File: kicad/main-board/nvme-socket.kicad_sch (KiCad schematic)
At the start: 8 parts, among them J5 Bus_M.2_Socket_M, U11 TPS22918DBVR

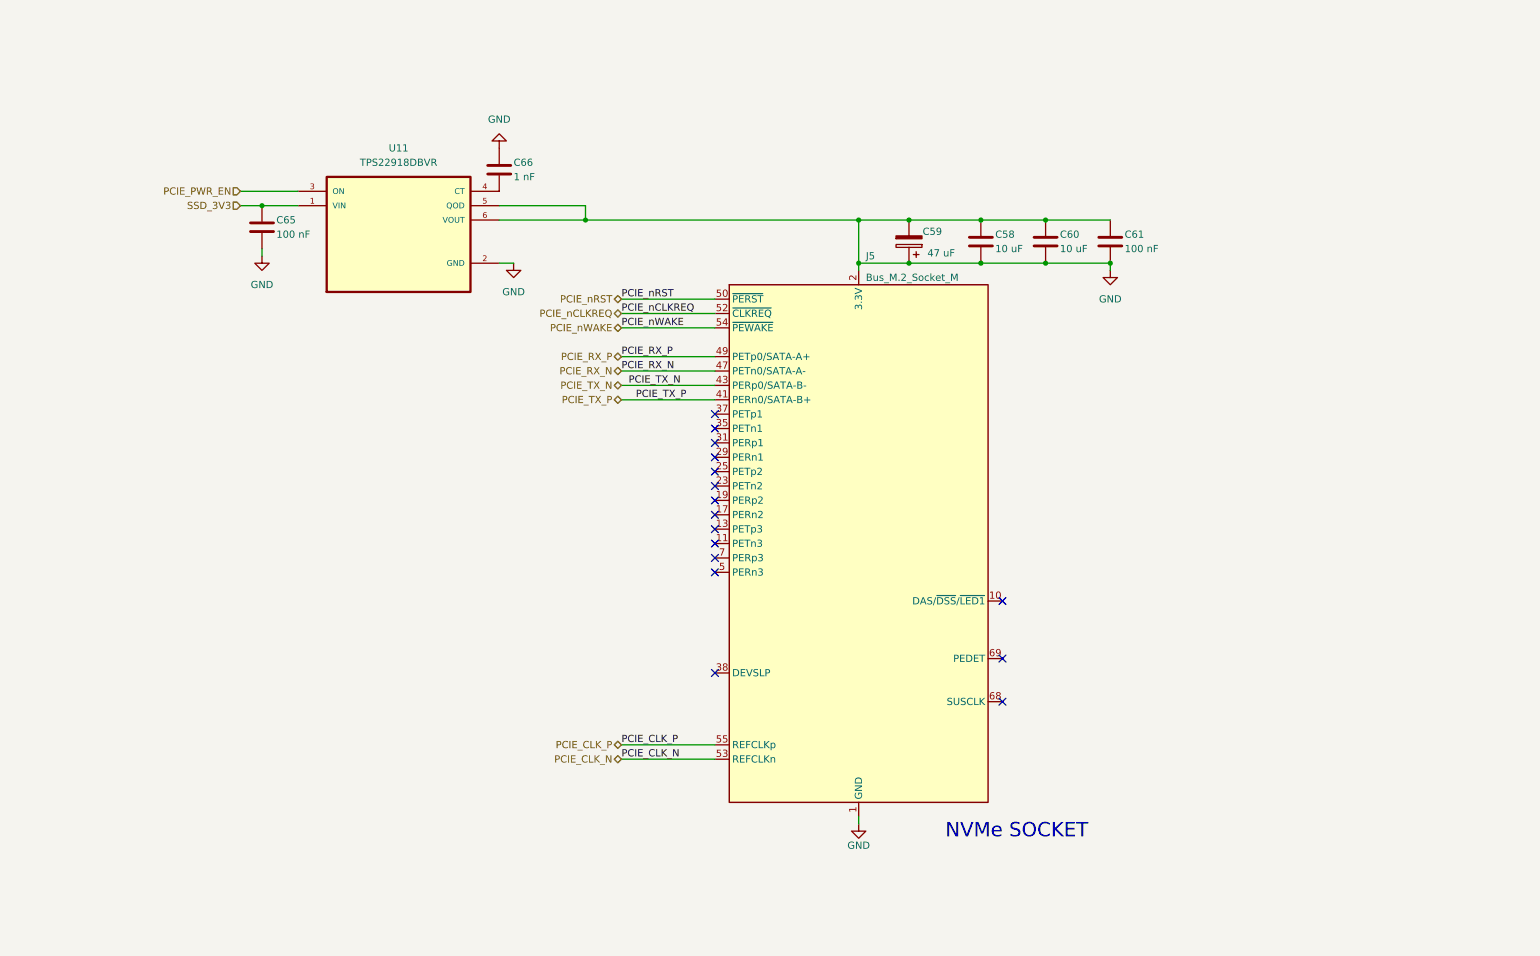
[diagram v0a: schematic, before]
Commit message: Completed the main board schematic
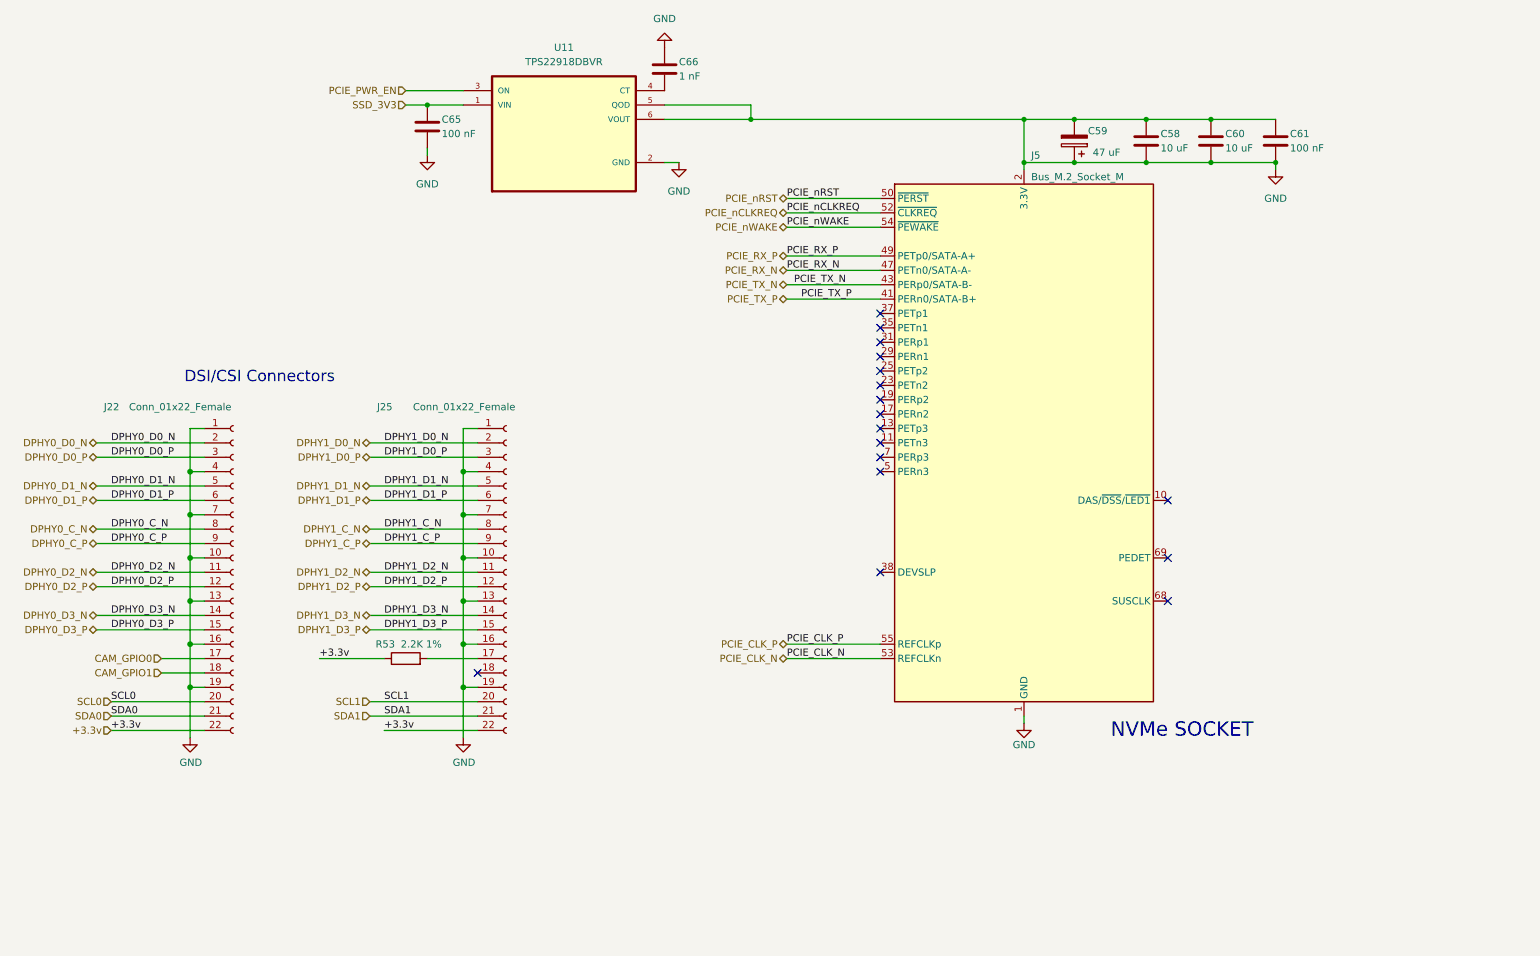
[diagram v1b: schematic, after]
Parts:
- added J22, J25: Conn_01x22_Female, CM5IO:Hirose_FH12-22S-0.5SH_1x22-1MP_P0.50mm_Horizontal, symbol Connector:Conn_01x22_Socket
- added R53: 2.2K 1%, Resistor_SMD:R_0402_1005Metric, symbol Device:R
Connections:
- net GND: now also J22.1 (Pin_1), J22.10 (Pin_10), J22.13 (Pin_13), J22.16 (Pin_16), J22.19 (Pin_19), J22.4 (Pin_4), J22.7 (Pin_7), J25.1 (Pin_1), J25.10 (Pin_10), J25.13 (Pin_13), J25.16 (Pin_16), J25.19 (Pin_19), J25.4 (Pin_4), J25.7 (Pin_7)
- new net: J25.17 (Pin_17), R53.2
- new net +3.3v: J22.22 (Pin_22), J25.22 (Pin_22), R53.1
- new net CAM_GPIO0: J22.17 (Pin_17)
- new net CAM_GPIO1: J22.18 (Pin_18)
- new net DPHY0_C_N: J22.8 (Pin_8)
- new net DPHY0_C_P: J22.9 (Pin_9)
- new net DPHY0_D0_N: J22.2 (Pin_2)
- new net DPHY0_D0_P: J22.3 (Pin_3)
- new net DPHY0_D1_N: J22.5 (Pin_5)
- new net DPHY0_D1_P: J22.6 (Pin_6)
- new net DPHY0_D2_N: J22.11 (Pin_11)
- new net DPHY0_D2_P: J22.12 (Pin_12)
- new net DPHY0_D3_N: J22.14 (Pin_14)
- new net DPHY0_D3_P: J22.15 (Pin_15)
- new net DPHY1_C_N: J25.8 (Pin_8)
- new net DPHY1_C_P: J25.9 (Pin_9)
- new net DPHY1_D0_N: J25.2 (Pin_2)
- new net DPHY1_D0_P: J25.3 (Pin_3)
- new net DPHY1_D1_N: J25.5 (Pin_5)
- new net DPHY1_D1_P: J25.6 (Pin_6)
- new net DPHY1_D2_N: J25.11 (Pin_11)
- new net DPHY1_D2_P: J25.12 (Pin_12)
- new net DPHY1_D3_N: J25.14 (Pin_14)
- new net DPHY1_D3_P: J25.15 (Pin_15)
- new net SCL0: J22.20 (Pin_20)
- new net SCL1: J25.20 (Pin_20)
- new net SDA0: J22.21 (Pin_21)
- new net SDA1: J25.21 (Pin_21)
- no-connect marks 16 -> 17
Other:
- note added: "DSI/CSI Connectors"
- moved on the sheet: C58, C59, C60, C61, C65, C66, J5, U11

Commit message: finally completed the schematic
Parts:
- renumbered C66 to C79, C65 to C80, C59 to C81, C58 to C82, C60 to C83, C61 to C84, J5 to J45, J22 to J46, J25 to J47, R53 to R69, U11 to U22
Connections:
- net GND: no longer C81.1, C82.1, C83.1, C84.1, J45.12 (3.3V), J45.14 (3.3V), J45.16 (3.3V), J45.18 (3.3V), J45.2 (3.3V), J45.4 (3.3V), J45.70 (3.3V), J45.72 (3.3V), J45.74 (3.3V), U22.5 (QOD), U22.6 (VOUT)
- net SSD_3V3 renamed SSD_3V
- new net: C81.1, C82.1, C83.1, C84.1, J45.12 (3.3V), J45.14 (3.3V), J45.16 (3.3V), J45.18 (3.3V), J45.2 (3.3V), J45.4 (3.3V), J45.70 (3.3V), J45.72 (3.3V), J45.74 (3.3V), U22.5 (QOD), U22.6 (VOUT)
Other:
- note added: "CIPHER - by ARYAN-GIT-BYTE"
- moved on the sheet: C81
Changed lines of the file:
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@@
 		(effects
 			(font
+				(face "Arial Black")
 				(size 2.0066 2.0066)
 			)
@@
 		(effects
 			(font
-				(face "KiCad Font")
+				(face "Arial Black")
 				(size 2.54 2.54)
 			)
 		)
 	)
+	(text "CIPHER - by ARYAN-GIT-BYTE\n"
+		(exclude_from_sim no)
+		(at 230.886 173.736 0)
+		(effects
+			(font
+				(face "Clarendon Lt BT")
+				(size 5.08 5.08)
+			)
+		)
+	)
 	(junction
 		(at 63.5 133.35)
@@
 	)
 	(junction
-		(at 210.82 40.64)
-		(diameter 0)
-		(color 0 0 0 0)
-	)
-	(junction
 		(at 63.5 125.73)
 		(diameter 1.016)
@@
 	)
 	(junction
-		(at 219.71 40.64)
+		(at 219.71 33.02)
 		(diameter 0)
 		(color 0 0 0 0)
@@
 	)
 	(junction
-		(at 219.71 33.02)
-		(diameter 0)
-		(color 0 0 0 0)
-	)
-	(junction
 		(at 111.76 102.87)
 		(diameter 1.016)
@@
 	(wire
 		(pts
-			(xy 219.71 33.02) (xy 232.41 33.02)
-		)
-		(stroke
-			(width 0)
-			(type default)
-		)
-	)
-	(wire
-		(pts
 			(xy 168.91 57.15) (xy 185.42 57.15)
 		)
@@
 	(wire
 		(pts
-			(xy 147.32 30.48) (xy 162.56 30.48)
-		)
-		(stroke
-			(width 0)
-			(type default)
-		)
-	)
-	(wire
-		(pts
 			(xy 95.25 113.03) (xy 114.3 113.03)
 		)
@@
 	(wire
 		(pts
-			(xy 210.82 40.64) (xy 219.71 40.64)
-		)
-		(stroke
-			(width 0)
-			(type default)
-		)
-	)
-	(wire
-		(pts
 			(xy 111.76 133.35) (xy 111.76 142.24)
 		)
@@
 	(wire
 		(pts
+			(xy 147.32 30.48) (xy 162.56 30.48)
+		)
+		(stroke
+			(width 0)
+			(type default)
+		)
+	)
+	(wire
+		(pts
 			(xy 63.5 125.73) (xy 66.04 125.73)
 		)
@@
 	(wire
 		(pts
-			(xy 210.82 33.02) (xy 210.82 40.64)
+			(xy 46.99 92.71) (xy 66.04 92.71)
 		)
 		(stroke
 			(width 0)
-			(type default)
+			(type solid)
 		)
 	)
 	(wire
 		(pts
-			(xy 46.99 92.71) (xy 66.04 92.71)
+			(xy 101.6 27.94) (xy 111.76 27.94)
 		)
 		(stroke
 			(width 0)
-			(type solid)
+			(type default)
 		)
 	)
 	(wire
 		(pts
-			(xy 101.6 27.94) (xy 111.76 27.94)
+			(xy 66.04 135.89) (xy 49.53 135.89)
 		)
 		(stroke
 			(width 0)
-			(type default)
+			(type solid)
 		)
 	)
 	(wire
 		(pts
-			(xy 66.04 135.89) (xy 49.53 135.89)
+			(xy 210.82 33.02) (xy 210.82 41.91)
 		)
 		(stroke
 			(width 0)
-			(type solid)
+			(type default)
 		)
 	)
 	(wire
 		(pts
-			(xy 210.82 40.64) (xy 210.82 41.91)
+			(xy 219.71 33.02) (xy 232.41 33.02)
 		)
 		(stroke
@@
 		)
 	)
-	(hierarchical_label "SSD_3V3"
+	(hierarchical_label "SSD_3V"
 		(shape input)
 		(at 101.6 30.48 180)
@@
 		(on_board yes)
 		(dnp no)
-		(property "Reference" "#PWR0134"
+		(property "Reference" "#PWR0129"
 			(at 63.5 148.59 0)
 			(effects
@@
 			(project "OVERALL"
 				(path "/0e81c85d-86ab-4d5d-8c59-60b8e6f89475/b23c6cec-f7d8-4bb5-9180-0d1142d1aed0/eea0b253-8fa4-41dd-9ad3-ca52a23a8c16/ed4211b6-8245-4b09-acae-1cf19e5170b7"
-					(reference "#PWR0134")
+					(reference "#PWR0129")
 					(unit 1)
 				)
@@
 		(on_board yes)
 		(dnp no)
-		(property "Reference" "#PWR0135"
+		(property "Reference" "#PWR0130"
 			(at 111.76 148.59 0)
 			(effects
@@
 			(project "OVERALL"
 				(path "/0e81c85d-86ab-4d5d-8c59-60b8e6f89475/b23c6cec-f7d8-4bb5-9180-0d1142d1aed0/eea0b253-8fa4-41dd-9ad3-ca52a23a8c16/ed4211b6-8245-4b09-acae-1cf19e5170b7"
-					(reference "#PWR0135")
+					(reference "#PWR0130")
 					(unit 1)
 				)
@@
 		(on_board yes)
 		(dnp no)
-		(property "Reference" "R53"
+		(property "Reference" "R69"
 			(at 99.695 125.73 90)
 			(effects
@@
 			(project "OVERALL"
 				(path "/0e81c85d-86ab-4d5d-8c59-60b8e6f89475/b23c6cec-f7d8-4bb5-9180-0d1142d1aed0/eea0b253-8fa4-41dd-9ad3-ca52a23a8c16/ed4211b6-8245-4b09-acae-1cf19e5170b7"
-					(reference "R53")
+					(reference "R69")
 					(unit 1)
 				)
@@
 		(on_board yes)
 		(dnp no)
-		(property "Reference" "C65"
+		(property "Reference" "C80"
 			(at 107.95 33.02 0)
 			(effects
@@
 			(project "OVERALL"
 				(path "/0e81c85d-86ab-4d5d-8c59-60b8e6f89475/b23c6cec-f7d8-4bb5-9180-0d1142d1aed0/eea0b253-8fa4-41dd-9ad3-ca52a23a8c16/ed4211b6-8245-4b09-acae-1cf19e5170b7"
-					(reference "C65")
+					(reference "C80")
 					(unit 1)
 				)
@@
 		(dnp no)
 		(fields_autoplaced yes)
-		(property "Reference" "#PWR067"
+		(property "Reference" "#PWR0116"
 			(at 149.86 46.99 0)
 			(effects
@@
 			(project ""
 				(path "/0e81c85d-86ab-4d5d-8c59-60b8e6f89475/b23c6cec-f7d8-4bb5-9180-0d1142d1aed0/eea0b253-8fa4-41dd-9ad3-ca52a23a8c16/ed4211b6-8245-4b09-acae-1cf19e5170b7"
-					(reference "#PWR067")
+					(reference "#PWR0116")
 					(unit 1)
 				)
@@
 		(dnp no)
 		(fields_autoplaced yes)
-		(property "Reference" "#PWR059"
+		(property "Reference" "#PWR0117"
 			(at 255.27 48.26 0)
 			(effects
@@
 			(project ""
 				(path "/0e81c85d-86ab-4d5d-8c59-60b8e6f89475/b23c6cec-f7d8-4bb5-9180-0d1142d1aed0/eea0b253-8fa4-41dd-9ad3-ca52a23a8c16/ed4211b6-8245-4b09-acae-1cf19e5170b7"
-					(reference "#PWR059")
+					(reference "#PWR0117")
 					(unit 1)
 				)
@@
 		(on_board yes)
 		(dnp no)
-		(property "Reference" "#PWR057"
+		(property "Reference" "#PWR0128"
 			(at 210.82 146.05 0)
 			(effects
@@
 			(project ""
 				(path "/0e81c85d-86ab-4d5d-8c59-60b8e6f89475/b23c6cec-f7d8-4bb5-9180-0d1142d1aed0/eea0b253-8fa4-41dd-9ad3-ca52a23a8c16/ed4211b6-8245-4b09-acae-1cf19e5170b7"
-					(reference "#PWR057")
+					(reference "#PWR0128")
 					(unit 1)
 				)
@@
 	(symbol
 		(lib_id "Device:C_Polarized")
-		(at 219.71 36.83 180)
+		(at 219.71 36.83 0)
 		(unit 1)
 		(exclude_from_sim no)
@@
 		(on_board yes)
 		(dnp no)
-		(property "Reference" "C59"
-			(at 225.552 35.052 0)
+		(property "Reference" "C81"
+			(at 220.726 34.798 0)
 			(effects
 				(font
@@
 		)
 		(property "Value" "47 uF"
-			(at 227.838 38.862 0)
+			(at 219.964 39.116 0)
 			(effects
 				(font
@@
 		)
 		(property "Footprint" ""
-			(at 218.7448 33.02 0)
+			(at 220.6752 40.64 0)
 			(effects
 				(font
@@
 			(project ""
 				(path "/0e81c85d-86ab-4d5d-8c59-60b8e6f89475/b23c6cec-f7d8-4bb5-9180-0d1142d1aed0/eea0b253-8fa4-41dd-9ad3-ca52a23a8c16/ed4211b6-8245-4b09-acae-1cf19e5170b7"
-					(reference "C59")
+					(reference "C81")
 					(unit 1)
 				)
@@
 		(dnp no)
 		(fields_autoplaced yes)
-		(property "Reference" "#PWR069"
+		(property "Reference" "#PWR0112"
 			(at 147.32 13.97 0)
 			(effects
@@
 			(project ""
 				(path "/0e81c85d-86ab-4d5d-8c59-60b8e6f89475/b23c6cec-f7d8-4bb5-9180-0d1142d1aed0/eea0b253-8fa4-41dd-9ad3-ca52a23a8c16/ed4211b6-8245-4b09-acae-1cf19e5170b7"
-					(reference "#PWR069")
+					(reference "#PWR0112")
 					(unit 1)
 				)
@@
 		(on_board yes)
 		(dnp no)
-		(property "Reference" "J22"
+		(property "Reference" "J46"
 			(at 48.26 83.82 0)
 			(effects
@@
 			(project "OVERALL"
 				(path "/0e81c85d-86ab-4d5d-8c59-60b8e6f89475/b23c6cec-f7d8-4bb5-9180-0d1142d1aed0/eea0b253-8fa4-41dd-9ad3-ca52a23a8c16/ed4211b6-8245-4b09-acae-1cf19e5170b7"
-					(reference "J22")
+					(reference "J46")
 					(unit 1)
 				)
@@
 		(on_board yes)
 		(dnp no)
-		(property "Reference" "J5"
+		(property "Reference" "J45"
 			(at 212.09 39.37 0)
 			(effects
@@
 			(project ""
 				(path "/0e81c85d-86ab-4d5d-8c59-60b8e6f89475/b23c6cec-f7d8-4bb5-9180-0d1142d1aed0/eea0b253-8fa4-41dd-9ad3-ca52a23a8c16/ed4211b6-8245-4b09-acae-1cf19e5170b7"
-					(reference "J5")
+					(reference "J45")
 					(unit 1)
 				)
@@
 		(on_board yes)
 		(dnp no)
-		(property "Reference" "J25"
+		(property "Reference" "J47"
 			(at 96.52 83.82 0)
 			(effects
@@
 			(project "OVERALL"
 				(path "/0e81c85d-86ab-4d5d-8c59-60b8e6f89475/b23c6cec-f7d8-4bb5-9180-0d1142d1aed0/eea0b253-8fa4-41dd-9ad3-ca52a23a8c16/ed4211b6-8245-4b09-acae-1cf19e5170b7"
-					(reference "J25")
+					(reference "J47")
 					(unit 1)
 				)
@@
 		(on_board yes)
 		(dnp no)
-		(property "Reference" "C66"
+		(property "Reference" "C79"
 			(at 149.86 22.86 0)
 			(effects
@@
 			(project "OVERALL"
 				(path "/0e81c85d-86ab-4d5d-8c59-60b8e6f89475/b23c6cec-f7d8-4bb5-9180-0d1142d1aed0/eea0b253-8fa4-41dd-9ad3-ca52a23a8c16/ed4211b6-8245-4b09-acae-1cf19e5170b7"
-					(reference "C66")
+					(reference "C79")
 					(unit 1)
 				)
@@
 		(on_board yes)
 		(dnp no)
-		(property "Reference" "C60"
+		(property "Reference" "C83"
 			(at 246.38 35.56 0)
 			(effects
@@
 			(project "OVERALL"
 				(path "/0e81c85d-86ab-4d5d-8c59-60b8e6f89475/b23c6cec-f7d8-4bb5-9180-0d1142d1aed0/eea0b253-8fa4-41dd-9ad3-ca52a23a8c16/ed4211b6-8245-4b09-acae-1cf19e5170b7"
-					(reference "C60")
+					(reference "C83")
 					(unit 1)
 				)
@@
 		(dnp no)
 		(fields_autoplaced yes)
-		(property "Reference" "#PWR068"
+		(property "Reference" "#PWR0115"
 			(at 105.41 45.72 0)
 			(effects
@@
 			(project ""
 				(path "/0e81c85d-86ab-4d5d-8c59-60b8e6f89475/b23c6cec-f7d8-4bb5-9180-0d1142d1aed0/eea0b253-8fa4-41dd-9ad3-ca52a23a8c16/ed4211b6-8245-4b09-acae-1cf19e5170b7"
-					(reference "#PWR068")
+					(reference "#PWR0115")
 					(unit 1)
 				)
@@
 		(on_board yes)
 		(dnp no)
-		(property "Reference" "C58"
+		(property "Reference" "C82"
 			(at 234.95 35.56 0)
 			(effects
@@
 			(project ""
 				(path "/0e81c85d-86ab-4d5d-8c59-60b8e6f89475/b23c6cec-f7d8-4bb5-9180-0d1142d1aed0/eea0b253-8fa4-41dd-9ad3-ca52a23a8c16/ed4211b6-8245-4b09-acae-1cf19e5170b7"
-					(reference "C58")
+					(reference "C82")
 					(unit 1)
 				)
@@
 		(dnp no)
 		(fields_autoplaced yes)
-		(property "Reference" "U11"
+		(property "Reference" "U22"
 			(at 129.54 20.32 0)
 			(effects
@@
 			(project ""
 				(path "/0e81c85d-86ab-4d5d-8c59-60b8e6f89475/b23c6cec-f7d8-4bb5-9180-0d1142d1aed0/eea0b253-8fa4-41dd-9ad3-ca52a23a8c16/ed4211b6-8245-4b09-acae-1cf19e5170b7"
-					(reference "U11")
+					(reference "U22")
 					(unit 1)
 				)
@@
 		(on_board yes)
 		(dnp no)
-		(property "Reference" "C61"
+		(property "Reference" "C84"
 			(at 257.81 35.56 0)
 			(effects
@@
 			(project "OVERALL"
 				(path "/0e81c85d-86ab-4d5d-8c59-60b8e6f89475/b23c6cec-f7d8-4bb5-9180-0d1142d1aed0/eea0b253-8fa4-41dd-9ad3-ca52a23a8c16/ed4211b6-8245-4b09-acae-1cf19e5170b7"
-					(reference "C61")
+					(reference "C84")
 					(unit 1)
 				)

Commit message: DOCUMENTED Till the Navigation board
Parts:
- renumbered C79 to C89, C80 to C90, C81 to C91, C82 to C92, C83 to C93, C84 to C94, J45 to J50, J46 to J51, J47 to J52, U22 to U24

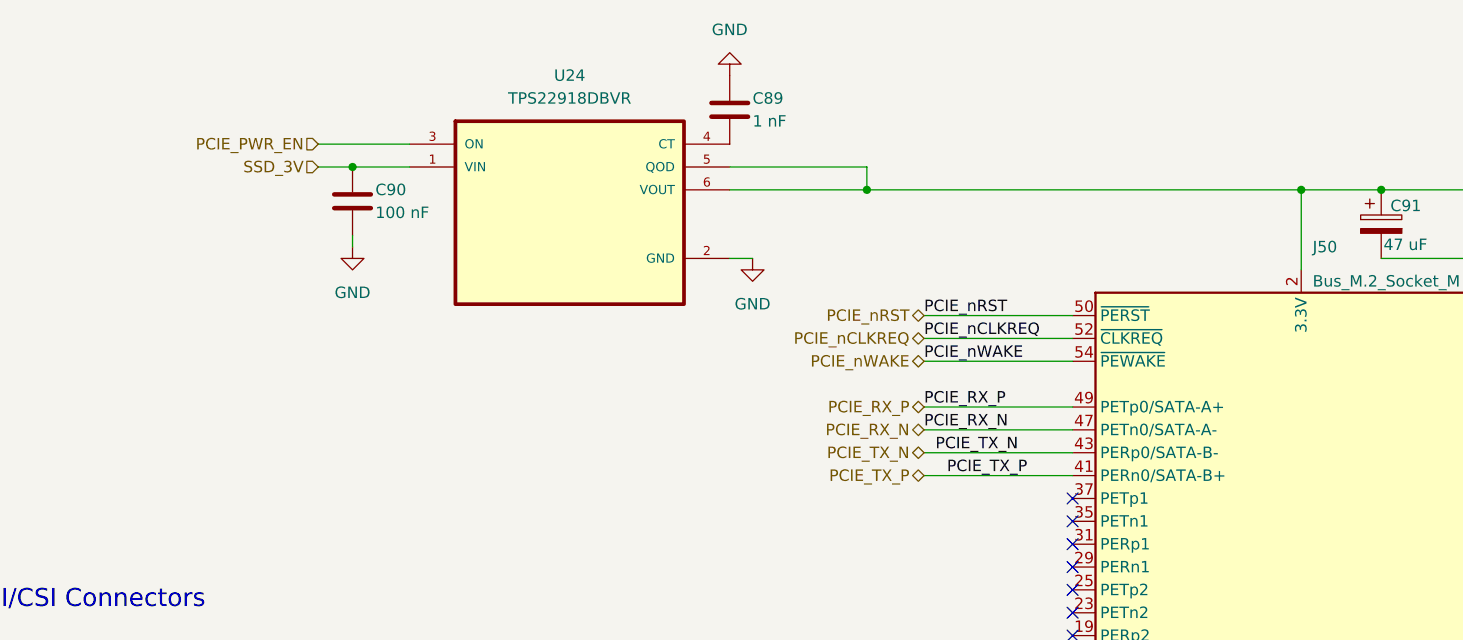
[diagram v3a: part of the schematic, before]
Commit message: migrating kicad 9 to 10
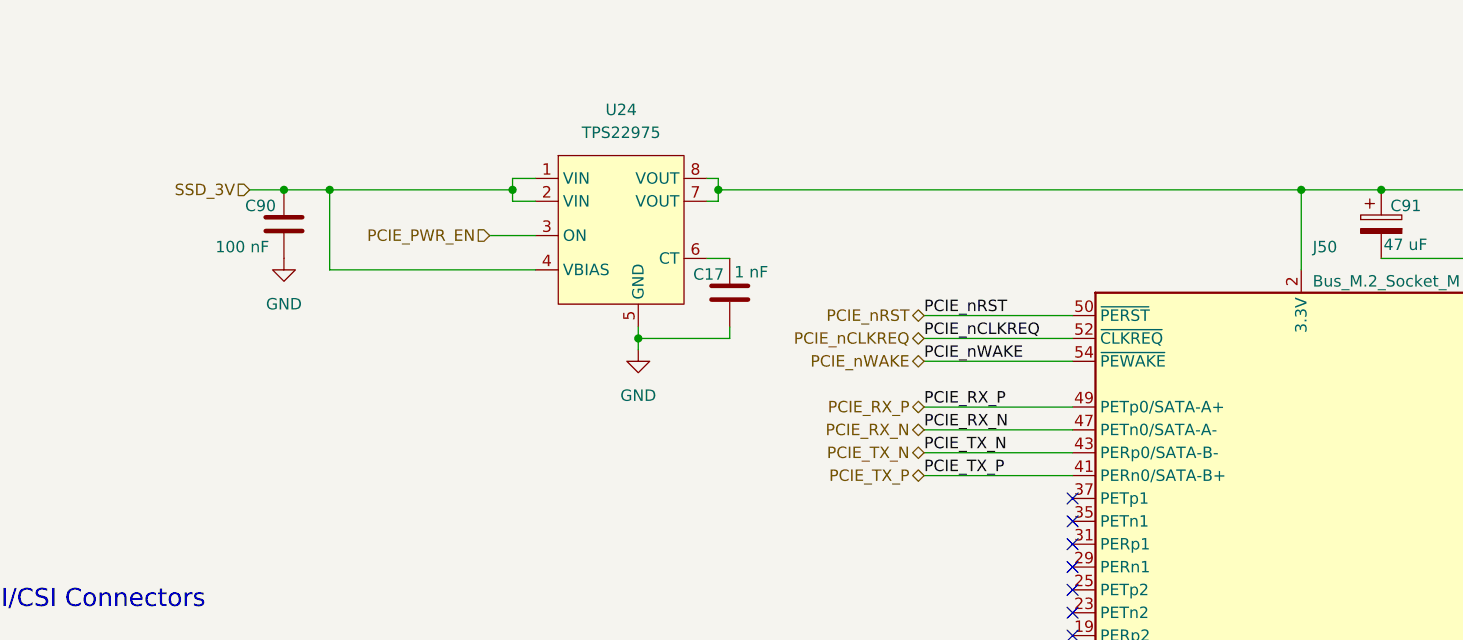
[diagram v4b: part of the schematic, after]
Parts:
- removed C89: 1 nF, symbol Device:C
- removed U24: TPS22918DBVR, TPS22918DBVR:SOT95P280X145-6N, symbol TPS22918DBVR:TPS22918DBVR
- added C17: 1 nF, symbol Device:C
- added U24: TPS22975, symbol TPS22975:TPS22975
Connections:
- net GND: now also C17.2, U24.5 (GND)
- net PCIE_PWR_EN: now also U24.3 (ON)
- net SSD_3V: now also U24.1 (VIN), U24.2 (VIN), U24.4 (VBIAS)
- net at C91.1, C92.1, C93.1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: now also U24.7 (VOUT), U24.8 (VOUT)
- new net: C17.1, U24.6 (CT)
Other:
- moved on the sheet: C90
